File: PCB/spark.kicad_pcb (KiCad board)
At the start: 4 copper layers, 82 x 55 mm, 202 parts, among them J1 USB_C_Receptacle, J11 Power Supply Out, J12 GPIO, J2 ADC_IN, J3 ST7789V, J4 Voltage Meter Thing, J5 USB_C_Receptacle, J6 Trackpad, J7 Digital Analyzer, Q1 STT6N3LLH6_C3021100, Q2 STT6N3LLH6_C3021100, Q3 BSS138, Q5 BSS138, SW1 SW_Push, SW2 SW_Push, U1 APS6404L-SQN-SN, U12 SL2.1A, U13 INA226, U14 TPS26630RGE, U17 TPS26630RGE, U19 USBLC6-2P6, U2 INA226, U20 AP63203WU, U21 W25Q128JVS, U24 RP2350A, U25 W25Q128JVS, U27 RP2350A, U3 SN74LVC8T245PWR, U4 SN74LVC8T245PWR, U5 IP2721, U6 MP8859GQ-0000-Z, Y2 ABM8-272-T3, Y4 ABM8-272-T3, Y5 ABM8-272-T3

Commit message: Fix MPN number, adjust footprint, production files
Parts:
- R53: footprint Resistor_SMD:R_0603_1608Metric -> Resistor_SMD:R_0402_1005Metric
- moved R53 0.15 mm to (174.1, 121.8)

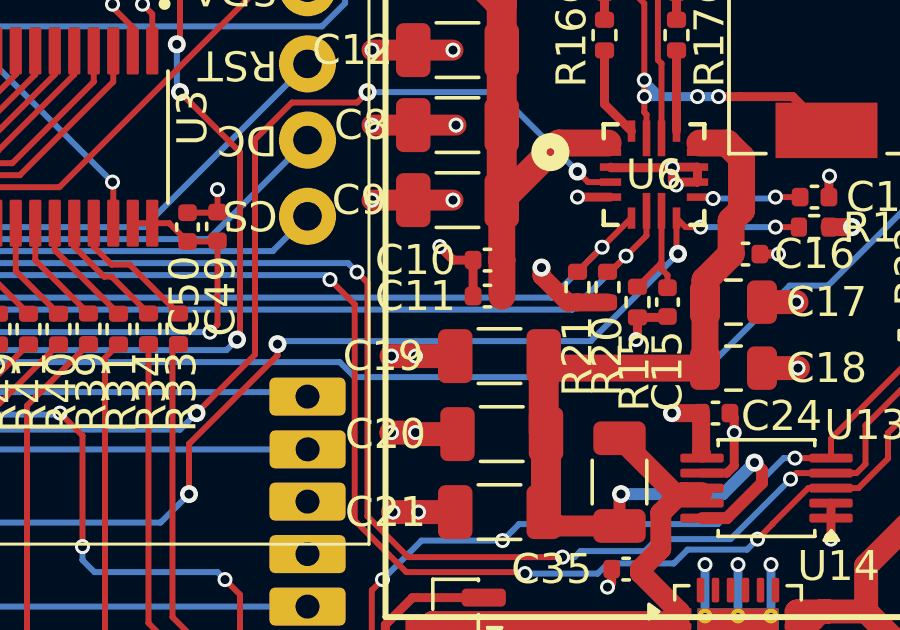
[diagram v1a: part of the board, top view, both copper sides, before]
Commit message: Add BOM and screenshots and cleanup. Updated PCB for fixed footprint for capacitor.
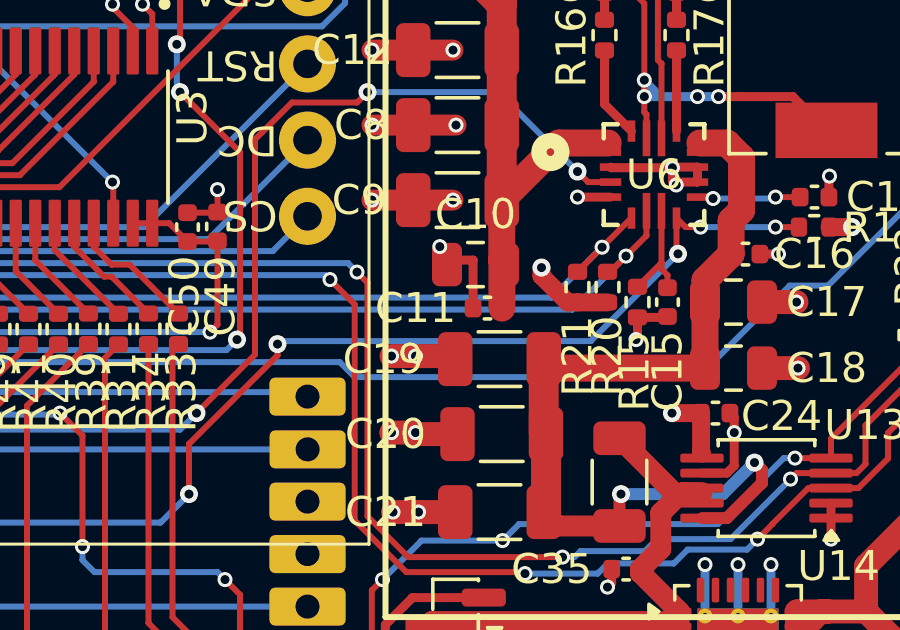
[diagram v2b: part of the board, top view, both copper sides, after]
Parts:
- C10: footprint Capacitor_SMD:C_0402_1005Metric -> Capacitor_SMD:C_0805_2012Metric
- moved C10 0.43 mm to (168.6, 105.8)
- moved C11 0.40 mm to (169.0, 107.2)
- moved C19 0.10 mm to (169.4, 108.9)
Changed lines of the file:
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@@
 	(footprint "Capacitor_SMD:C_1206_3216Metric"
 		(layer "F.Cu")
-		(at 169.4 108.8)
+		(at 169.4 108.9)
 		(descr "Capacitor SMD 1206 (3216 Metric), square (rectangular) end terminal, IPC-7351 nominal, (Body size source: IPC-SM-782 page 76, https://www.pcb-3d.com/wordpress/wp-content/uploads/ipc-sm-782a_amendment_1_and_2.pdf)")
 		(tags "capacitor")
@@
 		)
 	)
-	(footprint "Capacitor_SMD:C_0402_1005Metric"
+	(footprint "Capacitor_SMD:C_0805_2012Metric"
 		(layer "F.Cu")
-		(at 169 105.6)
-		(descr "Capacitor SMD 0402 (1005 Metric), square (rectangular) end terminal, IPC-7351 nominal, (Body size source: IPC-SM-782 page 76, https://www.pcb-3d.com/wordpress/wp-content/uploads/ipc-sm-782a_amendment_1_and_2.pdf)")
+		(at 168.6 105.75)
+		(descr "Capacitor SMD 0805 (2012 Metric), square (rectangular) end terminal, IPC-7351 nominal, (Body size source: IPC-SM-782 page 76, https://www.pcb-3d.com/wordpress/wp-content/uploads/ipc-sm-782a_amendment_1_and_2.pdf, https://docs.google.com/spreadsheets/d/1BsfQQcO9C6DZCsRaXUlFlo91Tg2WpOkGARC1WS5S8t0/edit?usp=sharing)")
 		(tags "capacitor")
 		(property "Reference" "C10"
-			(at -2.4 0 0)
+			(at 0 -1.68 0)
 			(layer "F.SilkS")
 			(effects
@@
 		)
 		(property "Value" "22uF 25V"
-			(at 0 1.16 0)
+			(at 0 1.68 0)
 			(layer "F.Fab")
-			(hide yes)
 			(effects
 				(font
@@
 			)
 		)
-		(property "MPN" "CGA2B2X7R1E223KT0Y0F"
+		(property "MPN" "CL21A226MAQNNNE"
 			(at 0 0 0)
 			(unlocked yes)
@@
 			)
 		)
-		(property "DESCRIPTION" ""
-			(at 0 0 0)
-			(unlocked yes)
-			(layer "F.Fab")
-			(hide yes)
-			(effects
-				(font
-					(size 1 1)
-					(thickness 0.15)
-				)
-			)
-		)
 		(property "OC_FARNELL" ""
 			(at 0 0 0)
@@
 		(duplicate_pad_numbers_are_jumpers no)
 		(fp_line
-			(start -0.107836 -0.36)
-			(end 0.107836 -0.36)
+			(start -0.261252 -0.735)
+			(end 0.261252 -0.735)
 			(stroke
 				(width 0.12)
@@
 		)
 		(fp_line
-			(start -0.107836 0.36)
-			(end 0.107836 0.36)
+			(start -0.261252 0.735)
+			(end 0.261252 0.735)
 			(stroke
 				(width 0.12)
@@
 		)
 		(fp_rect
-			(start -0.91 -0.46)
-			(end 0.91 0.46)
+			(start -1.7 -0.98)
+			(end 1.7 0.98)
 			(stroke
 				(width 0.05)
@@
 		)
 		(fp_rect
-			(start -0.5 -0.25)
-			(end 0.5 0.25)
+			(start -1 -0.625)
+			(end 1 0.625)
 			(stroke
 				(width 0.1)
@@
 			(effects
 				(font
-					(size 0.25 0.25)
-					(thickness 0.04)
+					(size 0.5 0.5)
+					(thickness 0.08)
 				)
 			)
 		)
 		(pad "1" smd roundrect
-			(at -0.48 0)
-			(size 0.56 0.62)
+			(at -0.95 0)
+			(size 1 1.45)
 			(layers "F.Cu" "F.Mask" "F.Paste")
 			(roundrect_rratio 0.25)
@@
 		)
 		(pad "2" smd roundrect
-			(at 0.48 0)
-			(size 0.56 0.62)
+			(at 0.95 0)
+			(size 1 1.45)
 			(layers "F.Cu" "F.Mask" "F.Paste")
 			(roundrect_rratio 0.25)
@@
 		)
 		(embedded_fonts no)
-		(model "${KICAD10_3DMODEL_DIR}/Capacitor_SMD.3dshapes/C_0402_1005Metric.step"
+		(model "${KICAD10_3DMODEL_DIR}/Capacitor_SMD.3dshapes/C_0805_2012Metric.step"
 			(offset
 				(xyz 0 0 0)
@@
 	(footprint "Capacitor_SMD:C_0402_1005Metric"
 		(layer "F.Cu")
-		(at 169 106.8)
+		(at 169 107.2)
 		(descr "Capacitor SMD 0402 (1005 Metric), square (rectangular) end terminal, IPC-7351 nominal, (Body size source: IPC-SM-782 page 76, https://www.pcb-3d.com/wordpress/wp-content/uploads/ipc-sm-782a_amendment_1_and_2.pdf)")
 		(tags "capacitor")
@@
 	)
 	(segment
-		(start 167.859702 105.6)
-		(end 167.409702 105.15)
-		(width 0.3)
-		(layer "F.Cu")
-		(net "GND")
-	)
-	(segment
 		(start 142.544975 111.616933)
 		(end 143.714975 112.786933)
@@
 	)
 	(segment
-		(start 168.52 105.6)
-		(end 167.859702 105.6)
-		(width 0.3)
-		(layer "F.Cu")
-		(net "GND")
-	)
-	(segment
 		(start 142.134976 107.666933)
 		(end 141.194975 108.606934)
@@
 	)
 	(segment
+		(start 167.825 108.8)
+		(end 166.6 108.8)
+		(width 0.8)
+		(layer "F.Cu")
+		(net "GND")
+	)
+	(segment
 		(start 159.289035 78.962957)
 		(end 159.288039 78.961961)
@@
 	)
 	(segment
-		(start 168.52 106.8)
-		(end 168.52 105.6)
-		(width 0.3)
-		(layer "F.Cu")
-		(net "GND")
-	)
-	(segment
 		(start 148.993891 95.576947)
 		(end 149.843053 95.576947)
@@
 	)
 	(segment
-		(start 167.925 108.8)
-		(end 166.6 108.8)
-		(width 0.8)
+		(start 168.52 107.2)
+		(end 168.52 105.6)
+		(width 0.3)
 		(layer "F.Cu")
 		(net "GND")
@@
 	)
 	(segment
+		(start 168.52 105.6)
+		(end 167.859702 105.6)
+		(width 0.3)
+		(layer "F.Cu")
+		(net "GND")
+	)
+	(segment
 		(start 166.65 111.4)
 		(end 166.6 111.35)
@@
 	)
 	(segment
+		(start 167.859702 105.6)
+		(end 167.409702 105.15)
+		(width 0.3)
+		(layer "F.Cu")
+		(net "GND")
+	)
+	(segment
 		(start 183.889678 77.485637)
 		(end 183.170765 76.766724)
@@
 	)
 	(segment
+		(start 167.925 108.9)
+		(end 167.825 108.8)
+		(width 0.8)
+		(layer "F.Cu")
+		(net "GND")
+	)
+	(segment
 		(start 149.32 82.21)
 		(end 149.35 82.18)
@@
 	)
 	(segment
-		(start 169.48 105.6)
-		(end 169.48 106.8)
-		(width 0.9)
-		(layer "F.Cu")
-		(net "VCC")
-	)
-	(segment
 		(start 168.7 95.1)
 		(end 168.7 94.05)
@@
 	)
 	(segment
-		(start 169.475 105.595)
-		(end 169.48 105.6)
-		(width 0.9)
-		(layer "F.Cu")
-		(net "VCC")
-	)
-	(segment
 		(start 152.45 76.45)
 		(end 151.9375 76.45)
@@
 	)
 	(segment
+		(start 169.475 105.595)
+		(end 169.48 105.6)
+		(width 0.9)
+		(layer "F.Cu")
+		(net "VCC")
+	)
+	(segment
 		(start 153.05 76.45)
 		(end 153.2 76.6)
@@
 	)
 	(segment
+		(start 169.48 105.6)
+		(end 169.48 107.2)
+		(width 0.9)
+		(layer "F.Cu")
+		(net "VCC")
+	)
+	(segment
 		(start 152.45 76.45)
 		(end 153.05 76.45)
@@
 	)
 	(segment
-		(start 171.275 109.2)
-		(end 170.875 108.8)
-		(width 0.9)
-		(layer "F.Cu")
-		(net "Net-(U13-Vin+)")
-	)
-	(segment
 		(start 177.46806 103.940154)
 		(end 177.46806 102.185459)
@@
 	)
 	(segment
-		(start 170.875 108.8)
-		(end 170.875 111.325)
-		(width 1)
-		(layer "F.Cu")
-		(net "Net-(U13-Vin+)")
-	)
-	(segment
-		(start 170.875 111.325)
-		(end 170.95 111.4)
-		(width 1)
+		(start 170.975 108.9)
+		(end 170.875 108.9)
+		(width 0.9)
 		(layer "F.Cu")
 		(net "Net-(U13-Vin+)")
@@
 	)
 	(segment
+		(start 176.25 109.2)
+		(end 171.275 109.2)
+		(width 0.9)
+		(layer "F.Cu")
+		(net "Net-(U13-Vin+)")
+	)
+	(segment
 		(start 170.95 111.4)
 		(end 170.95 113.925)
@@
 	)
 	(segment
+		(start 171.275 109.2)
+		(end 170.975 108.9)
+		(width 0.9)
+		(layer "F.Cu")
+		(net "Net-(U13-Vin+)")
+	)
+	(segment
 		(start 176.980601 101.698)
 		(end 176.077001 101.698)
@@
 	)
 	(segment
+		(start 170.875 111.325)
+		(end 170.95 111.4)
+		(width 1)
+		(layer "F.Cu")
+		(net "Net-(U13-Vin+)")
+	)
+	(segment
 		(start 177.12 105.4)
 		(end 177.12 104.288214)
@@
 	)
 	(segment
-		(start 176.25 109.2)
-		(end 171.275 109.2)
-		(width 0.9)
+		(start 170.875 108.9)
+		(end 170.875 111.325)
+		(width 1)
 		(layer "F.Cu")
 		(net "Net-(U13-Vin+)")
